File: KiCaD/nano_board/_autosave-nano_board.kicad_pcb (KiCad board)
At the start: 2 copper layers, 84 x 73.8 mm, 38 parts, among them J0 8P8C_Shielded, J1 Conn_02x05_Odd_Even, J2 LEMO2

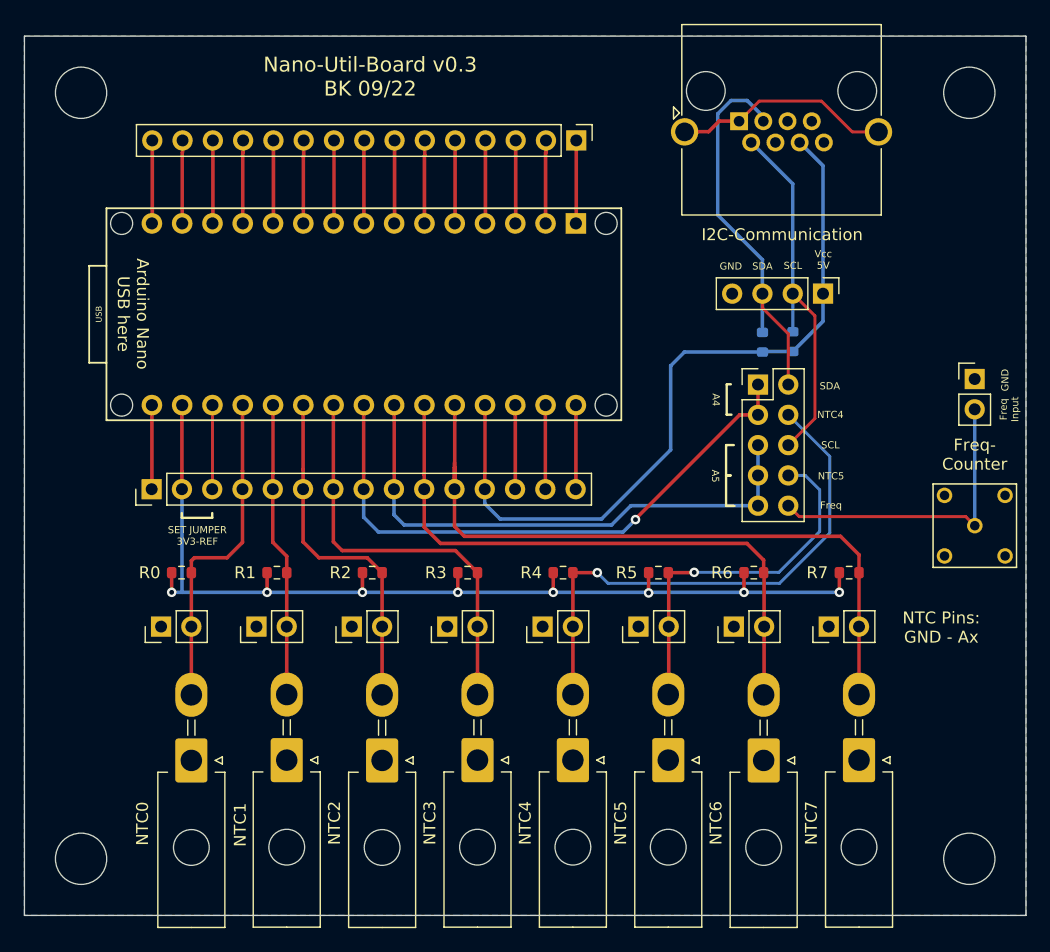
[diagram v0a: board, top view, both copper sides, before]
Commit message: ENH: rerouting and horizontal jumper selection
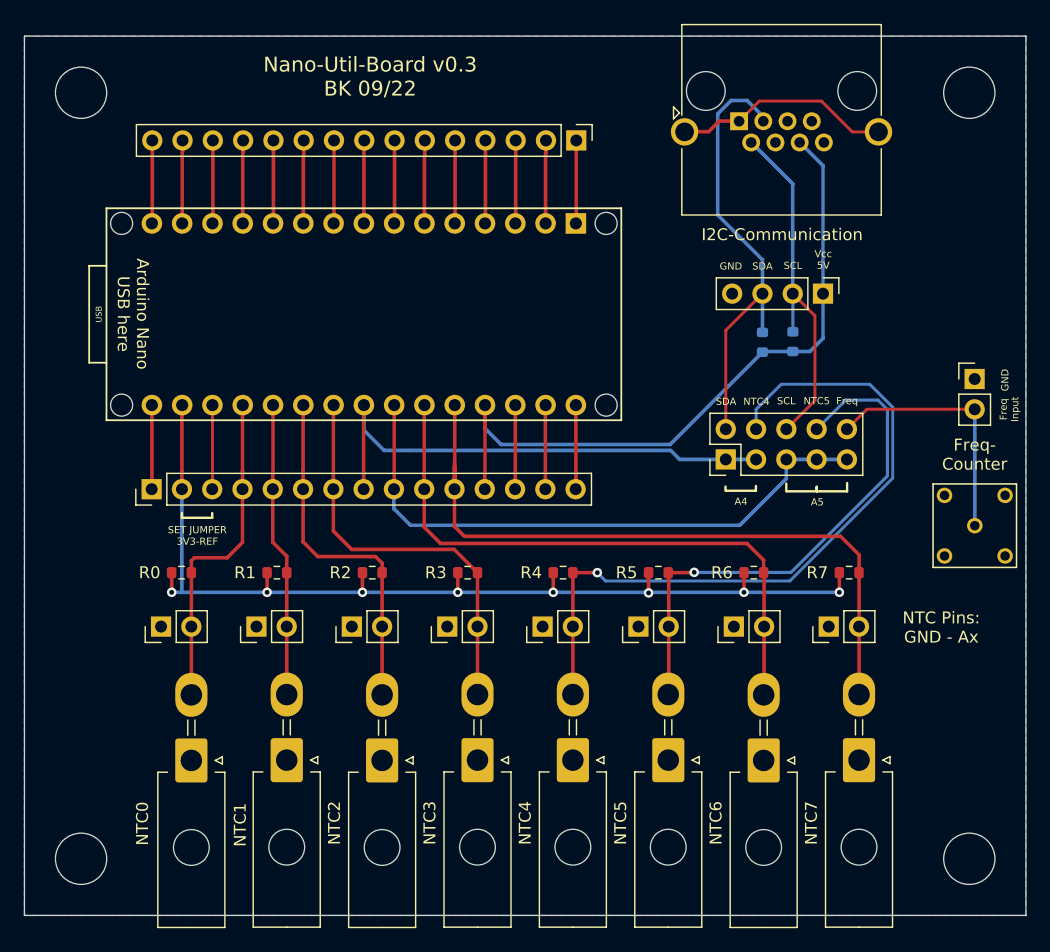
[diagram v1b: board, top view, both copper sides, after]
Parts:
- moved J1 6.84 mm to (148.8, 76.5), turned to 90 degrees
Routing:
- net N4: track 45.3 -> 61.6 mm
- net N5: track 30.9 -> 44.7 mm
- net A4: track 49.6 -> 43.0 mm, vias 1 -> 0
- net 5V_Ard: track 64.0 -> 58.8 mm
- net Freq: track 26.1 -> 21.2 mm
- net A5: track 45.8 -> 50.5 mm
- net SDA: track 33.3 -> 37.4 mm
- net SCL: track 31.7 -> 30.5 mm
- net A3: track 34.8 -> 34.3 mm
